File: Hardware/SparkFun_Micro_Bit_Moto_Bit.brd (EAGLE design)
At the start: 58.4 x 76.2 mm, 112 parts, among them J1 POWER_JACKPTH_LOCK, J10 Qwiic, J2 CORTEX_DEBUGPTH, U1 CY8C4245LQI-483, U2 TPS62172, U3 micro:bit, U4 DRV8835

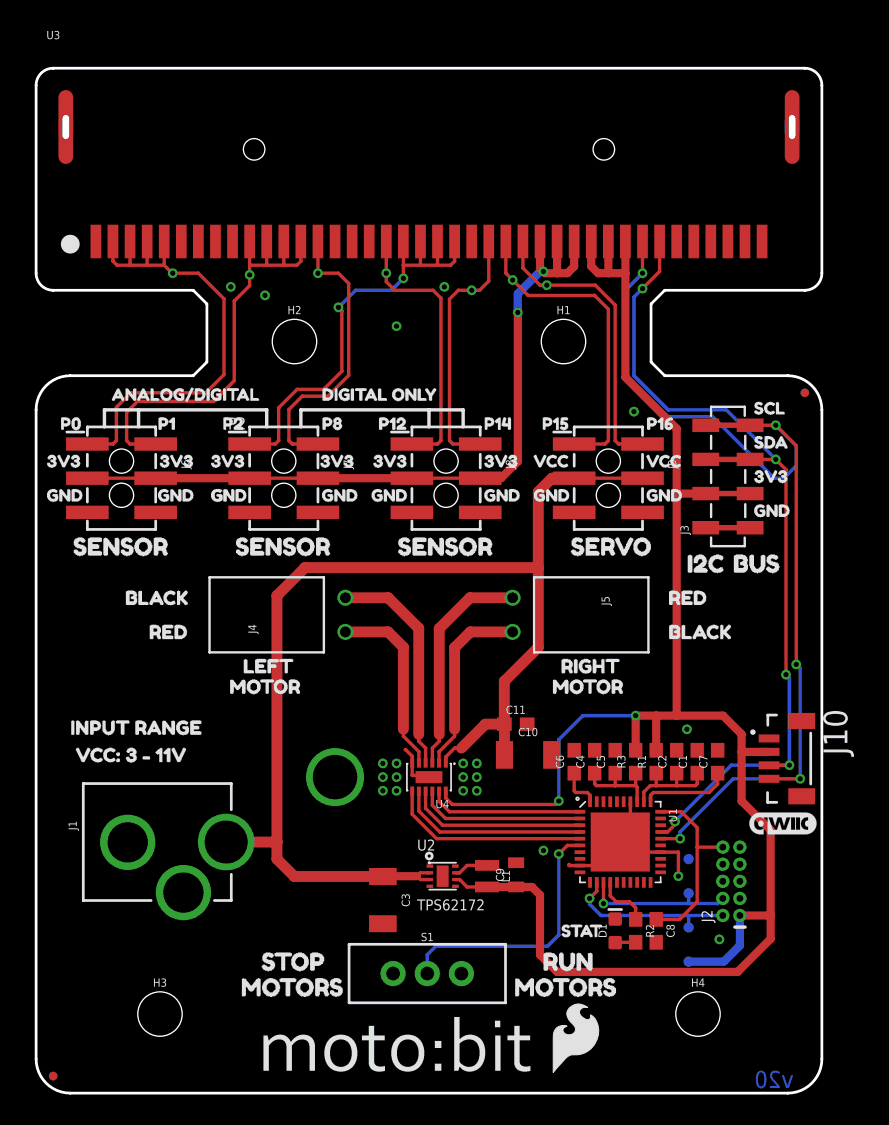
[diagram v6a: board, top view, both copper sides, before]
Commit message: Design review changes
Moved test points to line up with TB pogo pins
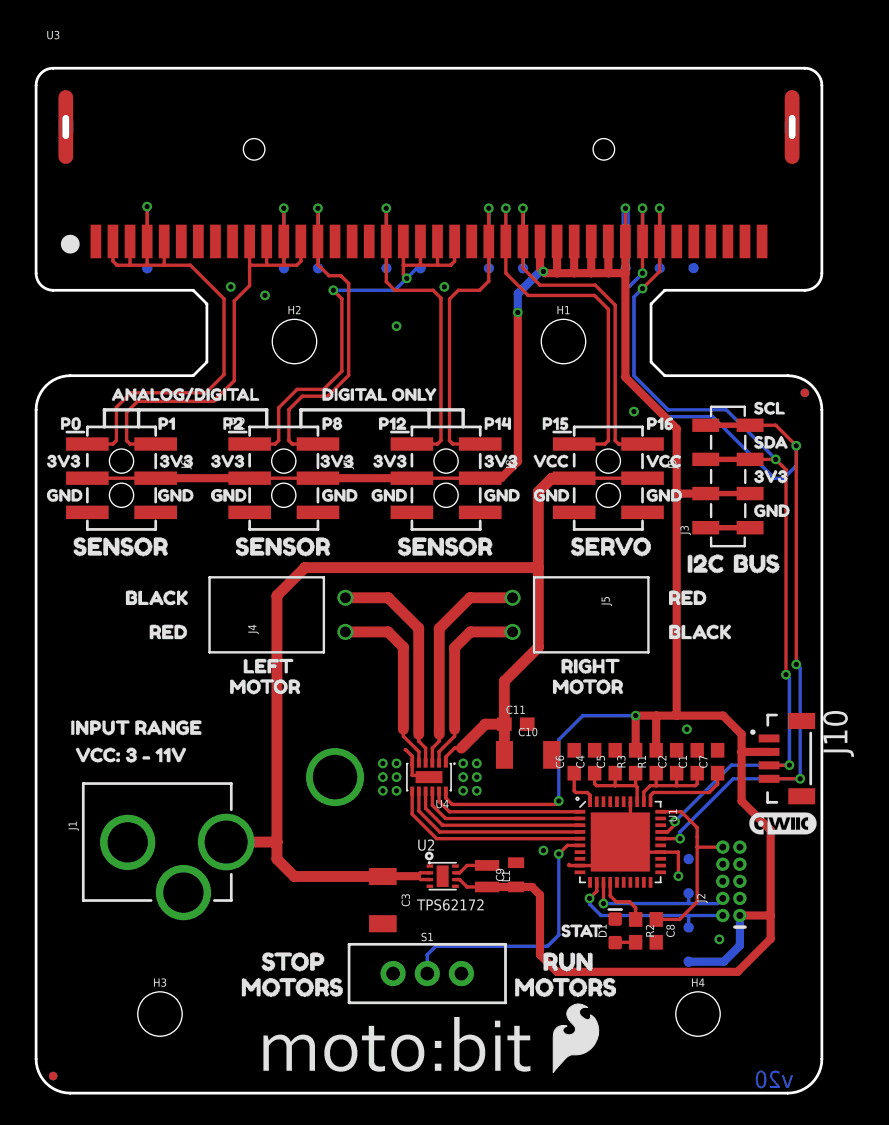
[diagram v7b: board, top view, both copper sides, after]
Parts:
- added TP15, TP16: (no value), SparkFun-Connectors:PAD.03X.03
- J2: value CORTEX_DEBUGPTH -> CORTEX_JTAG_DEBUG; device Pete_Connectors_Retired:2X5-PTH-1.27MM -> SparkFun-Connectors:2X5-PTH-1.27MM-NO_SILK
- TP10, TP11, TP12, TP13, TP14, TP5, TP6, TP7, TP8, TP9: device SparkFun-Connectors:TP_15TH -> SparkFun-Connectors:PAD.03X.03
- moved TP13 16.8 mm to (45.1, 63.2), flipped to the bottom
- moved TP14 16.6 mm to (46.4, 61.3), flipped to the bottom
- moved TP8 6.77 mm to (28.6, 61.3), flipped to the bottom
- moved TP11 2.84 mm to (34.9, 63.2), flipped to the bottom
- moved TP6 2.60 mm to (18.4, 61.3), flipped to the bottom
- moved TP12 2.17 mm to (36.2, 61.3), flipped to the bottom
- moved TP10 2.08 mm to (33.7, 61.3), flipped to the bottom
- moved TP5 1.93 mm to (8.27, 61.3), flipped to the bottom
- moved TP7 0.37 mm to (21.0, 61.3), flipped to the bottom
- moved TP9 0.37 mm to (26.0, 61.3), flipped to the bottom
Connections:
- net 3.3V: now also TP15.P$1
- net GND: now also TP16.P$1; no longer J2.7
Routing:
- net 3.3V: track 193.7 -> 202.1 mm, vias 4 -> 5
- net ANALOG_0: track 35.6 -> 42.7 mm, vias 0 -> 1
- net SDA: track 62.2 -> 69.2 mm, vias 4 -> 6
- net SERVO_16: track 22.2 -> 29.1 mm, vias 0 -> 1
- net DIGITAL_14: track 19.3 -> 26.3 mm, vias 0 -> 1
- net DIGITAL_12: track 20.4 -> 27.3 mm, vias 0 -> 1
- net ANALOG_1: track 33.2 -> 40.0 mm, vias 0 -> 1
- net DIGITAL_8: track 21.9 -> 28.4 mm, vias 0 -> 1
- net SERVO_15: track 23.5 -> 28.5 mm, vias 0 -> 1
- net ANALOG_2: track 32.8 -> 35.8 mm, vias 1 -> 2
- net SCL: track 77.4 -> 80.3 mm, vias 4 -> 6
